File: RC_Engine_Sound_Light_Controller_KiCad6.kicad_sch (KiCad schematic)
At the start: 44 parts, among them J1 RX, J10 RGB, J11 32, J12 CH1, J13 CH2, J14 CH3, J15 ESC, J16 CH4, J17 Brushed Motor output, J2 HeadL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

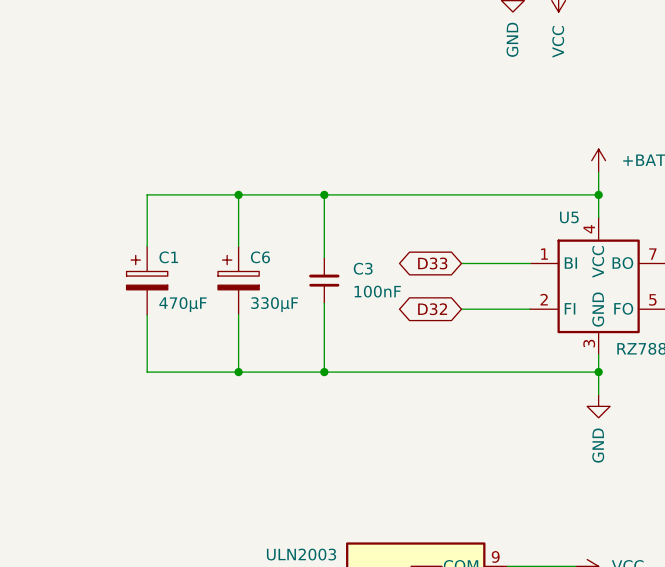
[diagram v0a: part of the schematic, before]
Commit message: Moved input capacitor 1 mm up and away from USB port.
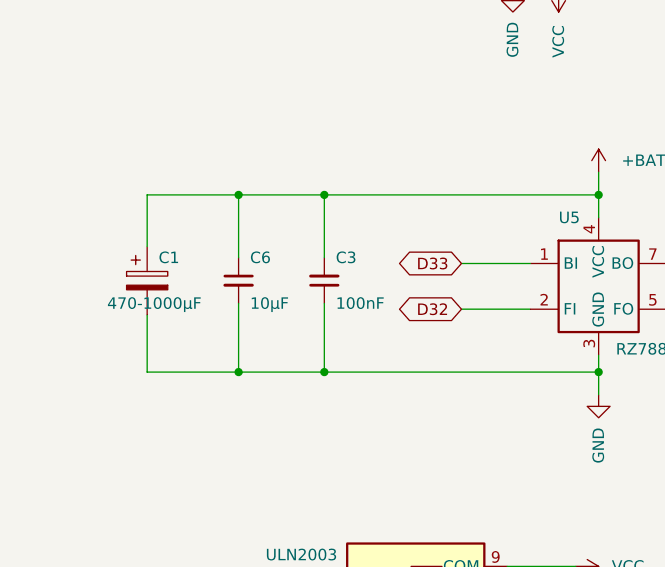
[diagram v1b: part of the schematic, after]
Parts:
- C1: value 470µF -> 470-1000µF
- C6: value 330µF -> 10µF; footprint Capacitor_Tantalum_SMD:CP_EIA-7343-30_AVX-N_Pad2.25x2.55mm_HandSolder -> Capacitor_SMD:C_1206_3216Metric_Pad1.33x1.80mm_HandSolder; symbol Device:C_Polarized -> Device:C_Small
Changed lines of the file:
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@@
     (stroke (width 0) (type default) (color 0 0 0 0))
   )
-  (wire (pts (xy 35.56 116.84) (xy 35.56 122.555))
+  (wire (pts (xy 35.56 116.84) (xy 35.56 123.825))
     (stroke (width 0) (type default) (color 0 0 0 0))
   )
@@
     (stroke (width 0) (type default) (color 0 0 0 0))
   )
-  (wire (pts (xy 35.56 130.175) (xy 35.56 136.525))
+  (wire (pts (xy 35.56 128.905) (xy 35.56 136.525))
     (stroke (width 0) (type default) (color 0 0 0 0))
   )
@@
   )
   (symbol (lib_id "Device:C_Small") (at 45.085 126.365 180) (unit 1)
-    (in_bom yes) (on_board yes) (fields_autoplaced)
-    (property "Reference" "C3" (id 0) (at 48.26 125.0885 0)
+    (in_bom yes) (on_board yes)
+    (property "Reference" "C3" (id 0) (at 46.355 123.825 0)
       (effects (font (size 1.27 1.27)) (justify right))
     )
-    (property "Value" "100nF" (id 1) (at 48.26 127.6285 0)
+    (property "Value" "100nF" (id 1) (at 46.355 128.905 0)
       (effects (font (size 1.27 1.27)) (justify right))
     )
@@
       (effects (font (size 1.27 1.27)) (justify left))
     )
-    (property "Value" "470µF" (id 1) (at 26.67 128.905 0)
+    (property "Value" "470-1000µF" (id 1) (at 20.955 128.905 0)
       (effects (font (size 1.27 1.27)) (justify left))
     )
@@
     (pin "1")
   )
-  (symbol (lib_id "Device:C_Polarized") (at 35.56 126.365 0) (unit 1)
+  (symbol (lib_id "Device:C_Small") (at 35.56 126.365 0) (unit 1)
     (in_bom yes) (on_board yes)
     (property "Reference" "C6" (id 0) (at 36.83 123.825 0)
       (effects (font (size 1.27 1.27)) (justify left))
     )
-    (property "Value" "330µF" (id 1) (at 36.83 128.905 0)
-      (effects (font (size 1.27 1.27)) (justify left))
-    )
-    (property "Footprint" "Capacitor_Tantalum_SMD:CP_EIA-7343-30_AVX-N_Pad2.25x2.55mm_HandSolder" (id 2) (at 36.5252 130.175 0)
+    (property "Value" "10µF" (id 1) (at 36.83 128.905 0)
+      (effects (font (size 1.27 1.27)) (justify left))
+    )
+    (property "Footprint" "Capacitor_SMD:C_1206_3216Metric_Pad1.33x1.80mm_HandSolder" (id 2) (at 35.56 126.365 0)
       (effects (font (size 1.27 1.27)) hide)
     )
@@
     )
     (path "/93facd0a-9e20-4d45-8a93-639a43f08d47"
-      (reference "C1") (unit 1) (value "470µF") (footprint "Capacitor_THT:CP_Radial_D10.0mm_P2.50mm_P5.00mm")
+      (reference "C1") (unit 1) (value "470-1000µF") (footprint "Capacitor_THT:CP_Radial_D10.0mm_P2.50mm_P5.00mm")
     )
     (path "/774cdfe1-0d63-4ebf-b755-ac1cbb67570a"
@@
     )
     (path "/d6b2c705-288c-461d-a44d-5ccfd9bf4ed2"
-      (reference "C6") (unit 1) (value "330µF") (footprint "Capacitor_Tantalum_SMD:CP_EIA-7343-30_AVX-N_Pad2.25x2.55mm_HandSolder")
+      (reference "C6") (unit 1) (value "10µF") (footprint "Capacitor_SMD:C_1206_3216Metric_Pad1.33x1.80mm_HandSolder")
     )
     (path "/5e1c7cd0-d026-4953-a288-7f9b38fc96fd"

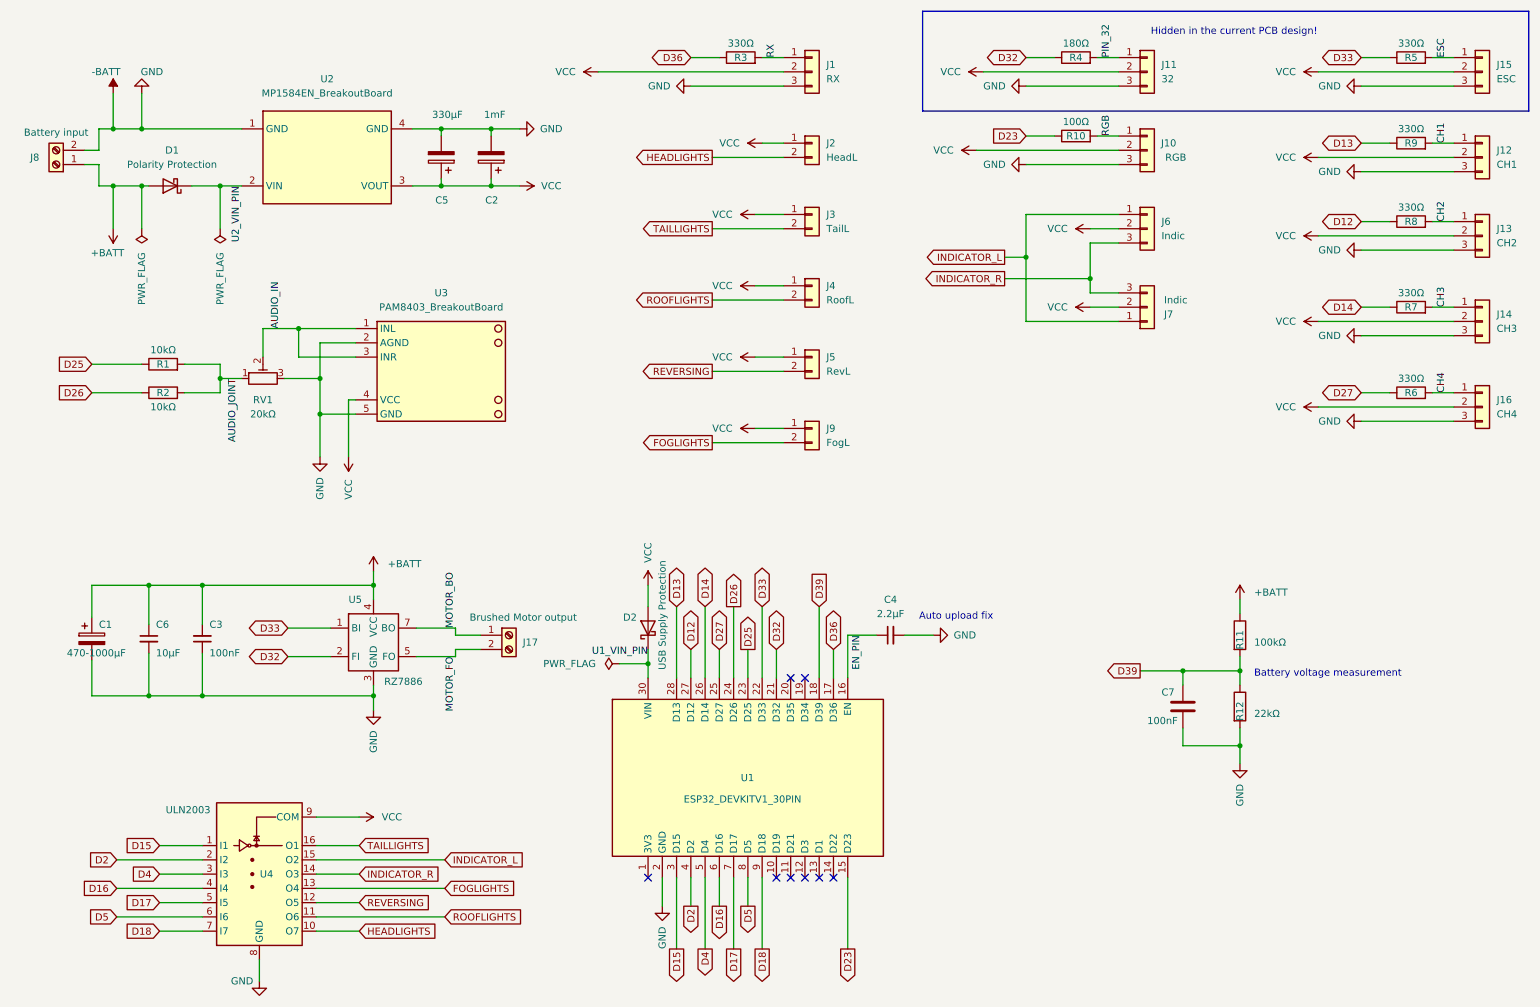
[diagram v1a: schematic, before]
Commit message: Added solder jumper between VCC and VDD.
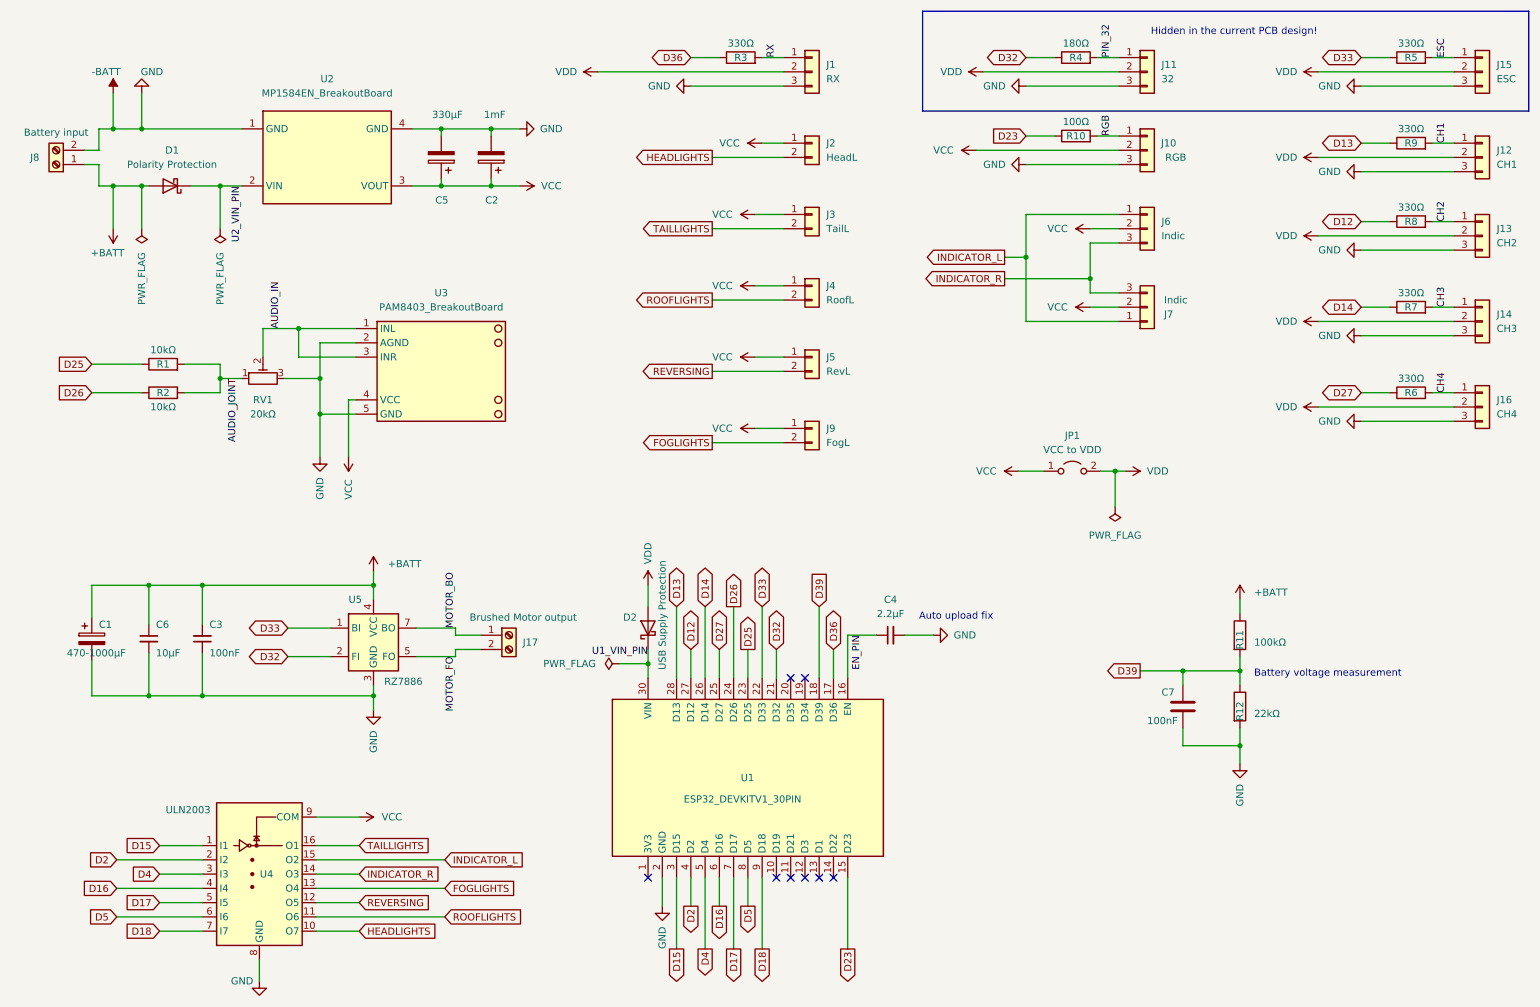
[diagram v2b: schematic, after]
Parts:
- added JP1: VCC to VDD, Jumper:SolderJumper-2_P1.3mm_Open_TrianglePad1.0x1.5mm, symbol Jumper:Jumper_2_Open
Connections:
- net VCC: now also JP1.1 (A); no longer D2.2 (A), J1.2 (Pin_2), J11.2 (Pin_2), J12.2 (Pin_2), J13.2 (Pin_2), J14.2 (Pin_2), J15.2 (Pin_2), J16.2 (Pin_2)
- new net VDD: D2.2 (A), J1.2 (Pin_2), J11.2 (Pin_2), J12.2 (Pin_2), J13.2 (Pin_2), J14.2 (Pin_2), J15.2 (Pin_2), J16.2 (Pin_2), JP1.2 (B)

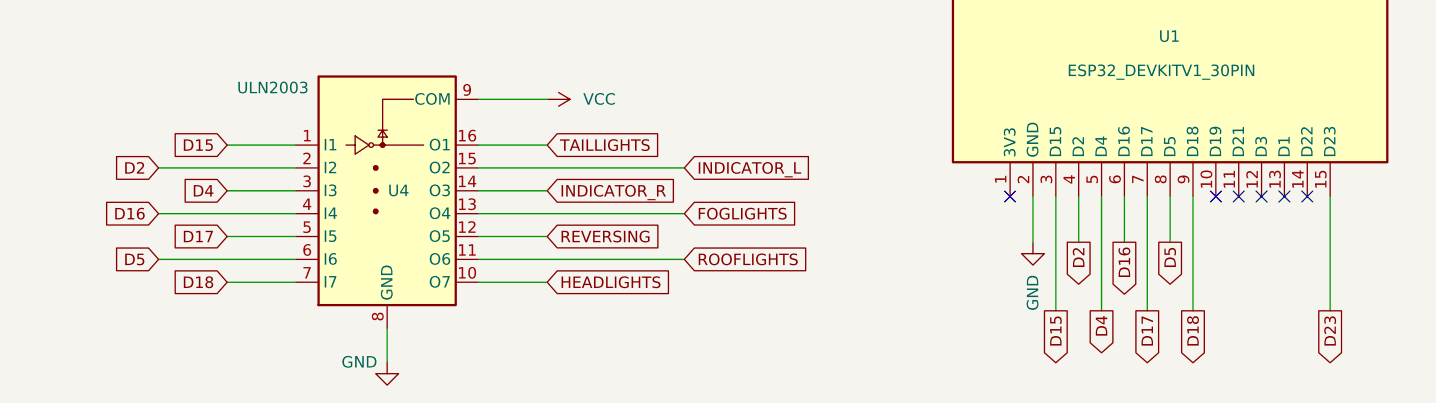
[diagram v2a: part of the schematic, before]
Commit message: Fixed wrong headlight pin (moved from D18 to D3).
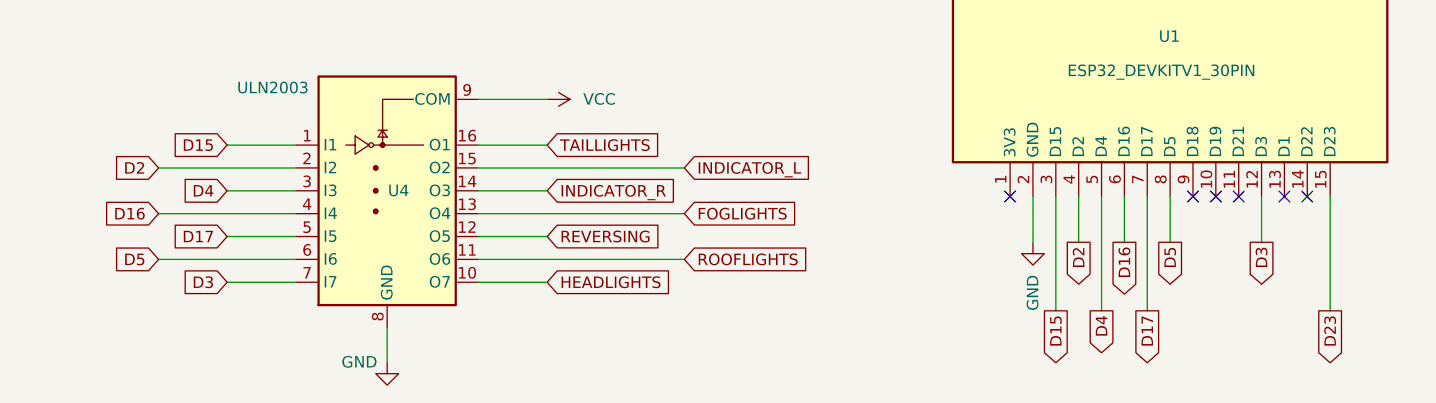
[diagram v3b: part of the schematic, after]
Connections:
- net D3: now reaches U1.12 (D3)
- net D3: now also U4.7 (I7)
- net D18: no longer names the net of U1.9 (D18)
- net D18: no longer U4.7 (I7)
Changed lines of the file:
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@@
   (no_connect (at 149.86 133.35))
   (no_connect (at 149.86 168.91))
-  (no_connect (at 152.4 168.91))
   (no_connect (at 154.94 168.91))
   (no_connect (at 157.48 168.91))
   (no_connect (at 147.32 168.91))
   (no_connect (at 152.4 133.35))
+  (no_connect (at 144.78 168.91))
   (no_connect (at 124.46 168.91))
   (wire (pts (xy 26.67 45.72) (xy 29.21 45.72))
@@
     (stroke (width 0) (type default) (color 0 0 0 0))
   )
-  (wire (pts (xy 144.78 168.91) (xy 144.78 181.61))
+  (wire (pts (xy 152.4 168.91) (xy 152.4 173.99))
     (stroke (width 0) (type default) (color 0 0 0 0))
   )
@@
     )
   )
-  (global_label "D18" (shape output) (at 144.78 181.61 270) (fields_autoplaced)
-    (effects (font (size 1.27 1.27)) (justify right))
-    (property "Intersheet References" "${INTERSHEET_REFS}" (id 0) (at 144.7006 187.7121 90)
+  (global_label "D3" (shape output) (at 152.4 173.99 270) (fields_autoplaced)
+    (effects (font (size 1.27 1.27)) (justify right))
+    (property "Intersheet References" "${INTERSHEET_REFS}" (id 0) (at 152.3206 178.8826 90)
       (effects (font (size 1.27 1.27)) (justify right) hide)
     )
@@
     )
   )
-  (global_label "D18" (shape input) (at 37.465 178.435 180) (fields_autoplaced)
-    (effects (font (size 1.27 1.27)) (justify right))
-    (property "Intersheet References" "${INTERSHEET_REFS}" (id 0) (at 31.3629 178.3556 0)
-      (effects (font (size 1.27 1.27)) (justify right) hide)
-    )
+  (global_label "D3" (shape input) (at 37.465 178.435 180) (fields_autoplaced)
+    (effects (font (size 1.27 1.27)) (justify right))
+    (property "Intersheet References" "${INTERSHEET_REFS}" (id 0) (at 32.5724 178.3556 0)
+      (effects (font (size 1.27 1.27)) (justify right) hide)
+    )

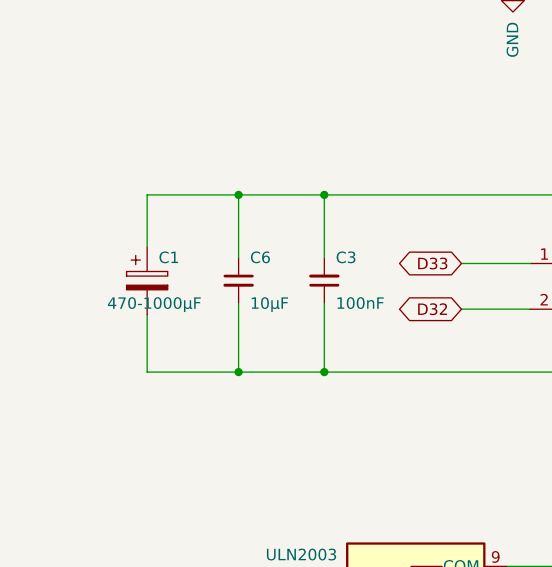
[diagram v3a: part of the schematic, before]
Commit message: Audio traces optimized. Added small ceramic capacitor at driver IC.
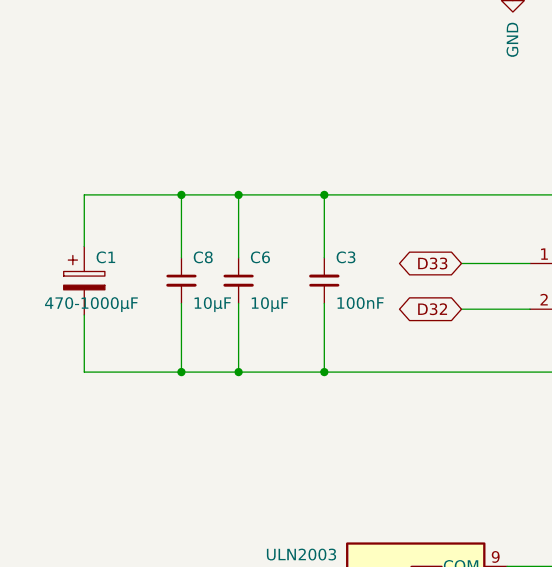
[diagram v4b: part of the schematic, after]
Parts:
- added C8: 10µF, Capacitor_SMD:C_1206_3216Metric_Pad1.33x1.80mm_HandSolder, symbol Device:C_Small
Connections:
- net +BATT: now also C8.1
- net -BATT: now also C8.2
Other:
- moved on the sheet: C1
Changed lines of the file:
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@@
   (junction (at 34.29 35.56) (diameter 0) (color 0 0 0 0)
   )
+  (junction (at 29.21 136.525) (diameter 0) (color 0 0 0 0)
+  )
   (junction (at 45.085 116.84) (diameter 0) (color 0 0 0 0)
   )
@@
   )
   (junction (at 229.87 145.415) (diameter 0) (color 0 0 0 0)
+  )
+  (junction (at 29.21 116.84) (diameter 0) (color 0 0 0 0)
   )
   (junction (at 203.2 62.23) (diameter 0) (color 0 0 0 0)
@@
     (stroke (width 0) (type default) (color 0 0 0 0))
   )
+  (wire (pts (xy 29.21 128.905) (xy 29.21 136.525))
+    (stroke (width 0) (type default) (color 0 0 0 0))
+  )
   (wire (pts (xy 203.2 62.23) (xy 203.2 55.88))
     (stroke (width 0) (type default) (color 0 0 0 0))
@@
     (stroke (width 0) (type default) (color 0 0 0 0))
   )
+  (wire (pts (xy 29.21 116.84) (xy 29.21 123.825))
+    (stroke (width 0) (type default) (color 0 0 0 0))
+  )
   (wire (pts (xy 190.5 96.52) (xy 194.945 96.52))
     (stroke (width 0) (type default) (color 0 0 0 0))
   )
-  (wire (pts (xy 25.4 136.525) (xy 35.56 136.525))
+  (wire (pts (xy 18.415 136.525) (xy 29.21 136.525))
     (stroke (width 0) (type default) (color 0 0 0 0))
   )
@@
     (stroke (width 0) (type default) (color 0 0 0 0))
   )
-  (wire (pts (xy 25.4 116.84) (xy 35.56 116.84))
+  (wire (pts (xy 18.415 116.84) (xy 29.21 116.84))
     (stroke (width 0) (type default) (color 0 0 0 0))
   )
@@
     (stroke (width 0) (type default) (color 0 0 0 0))
   )
-  (wire (pts (xy 25.4 116.84) (xy 25.4 122.555))
+  (wire (pts (xy 18.415 116.84) (xy 18.415 122.555))
     (stroke (width 0) (type default) (color 0 0 0 0))
   )
@@
     (stroke (width 0) (type default) (color 0 0 0 0))
   )
-  (wire (pts (xy 25.4 136.525) (xy 25.4 130.175))
+  (wire (pts (xy 18.415 136.525) (xy 18.415 130.175))
     (stroke (width 0) (type default) (color 0 0 0 0))
   )
@@
     (stroke (width 0) (type default) (color 0 0 0 0))
   )
+  (wire (pts (xy 29.21 116.84) (xy 35.56 116.84))
+    (stroke (width 0) (type default) (color 0 0 0 0))
+  )
   (wire (pts (xy 142.24 128.27) (xy 142.24 133.35))
     (stroke (width 0) (type default) (color 0 0 0 0))
@@
   )
   (wire (pts (xy 251.46 52.07) (xy 256.54 52.07))
+    (stroke (width 0) (type default) (color 0 0 0 0))
+  )
+  (wire (pts (xy 29.21 136.525) (xy 35.56 136.525))
     (stroke (width 0) (type default) (color 0 0 0 0))
   )
@@
     (pin "2")
   )
-  (symbol (lib_id "Device:C_Polarized") (at 25.4 126.365 0) (unit 1)
-    (in_bom yes) (on_board yes)
-    (property "Reference" "C1" (id 0) (at 26.67 123.825 0)
-      (effects (font (size 1.27 1.27)) (justify left))
-    )
-    (property "Value" "470-1000µF" (id 1) (at 20.955 128.905 0)
-      (effects (font (size 1.27 1.27)) (justify left))
-    )
-    (property "Footprint" "Capacitor_THT:CP_Radial_D10.0mm_P2.50mm_P5.00mm" (id 2) (at 26.3652 130.175 0)
-      (effects (font (size 1.27 1.27)) hide)
-    )
-    (property "Datasheet" "~" (id 3) (at 25.4 126.365 0)
+  (symbol (lib_id "Device:C_Polarized") (at 18.415 126.365 0) (unit 1)
+    (in_bom yes) (on_board yes)
+    (property "Reference" "C1" (id 0) (at 19.685 123.825 0)
+      (effects (font (size 1.27 1.27)) (justify left))
+    )
+    (property "Value" "470-1000µF" (id 1) (at 13.97 128.905 0)
+      (effects (font (size 1.27 1.27)) (justify left))
+    )
+    (property "Footprint" "Capacitor_THT:CP_Radial_D10.0mm_P2.50mm_P5.00mm" (id 2) (at 19.3802 130.175 0)
+      (effects (font (size 1.27 1.27)) hide)
+    )
+    (property "Datasheet" "~" (id 3) (at 18.415 126.365 0)
       (effects (font (size 1.27 1.27)) hide)
     )
@@
     (pin "2")
   )
+  (symbol (lib_id "Device:C_Small") (at 29.21 126.365 0) (unit 1)
+    (in_bom yes) (on_board yes)
+    (property "Reference" "C8" (id 0) (at 30.48 123.825 0)
+      (effects (font (size 1.27 1.27)) (justify left))
+    )
+    (property "Value" "10µF" (id 1) (at 30.48 128.905 0)
+      (effects (font (size 1.27 1.27)) (justify left))
+    )
+    (property "Footprint" "Capacitor_SMD:C_1206_3216Metric_Pad1.33x1.80mm_HandSolder" (id 2) (at 29.21 126.365 0)
+      (effects (font (size 1.27 1.27)) hide)
+    )
+    (property "Datasheet" "~" (id 3) (at 29.21 126.365 0)
+      (effects (font (size 1.27 1.27)) hide)
+    )
+    (pin "1")
+    (pin "2")
+  )
   (symbol (lib_id "Connector_Generic:Conn_01x02") (at 153.67 38.1 0) (unit 1)
     (in_bom yes) (on_board yes) (fields_autoplaced)
@@
       (reference "C7") (unit 1) (value "100nF") (footprint "Capacitor_SMD:C_1206_3216Metric_Pad1.33x1.80mm_HandSolder")
     )
+    (path "/f210dacd-f6db-4226-9ada-d73fe606b2db"
+      (reference "C8") (unit 1) (value "10µF") (footprint "Capacitor_SMD:C_1206_3216Metric_Pad1.33x1.80mm_HandSolder")
+    )
     (path "/eca3bb7b-a37d-4395-81c5-81f63a2b25c0"
